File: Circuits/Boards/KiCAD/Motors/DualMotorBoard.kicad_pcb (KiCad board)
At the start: 2 copper layers, 127 x 101.6 mm, 96 parts, among them J1 Conn_01x05, J10 Conn_01x01, J11 Conn_01x01, J12 Conn_01x01, J13 Conn_01x01, J14 Conn_01x01, J2 Conn_01x01, J3 Conn_01x01, J4 Conn_01x01, J5 Conn_01x01, J6 Conn_01x01, J7 Conn_01x01, J8 Conn_01x05, J9 Conn_01x01, Q1 2N3904, Q10 Q_NMOS_DGS, Q11 Q_NMOS_DGS, Q12 Q_NMOS_DGS, Q13 Q_NMOS_DGS, Q14 2N3904, Q15 2N3904, Q16 2N3904, Q17 2N3904, Q18 2N3904, Q19 2N3904, Q2 2N3904, Q20 2N3904, Q21 2N3904, Q22 2N3904, Q23 Q_NMOS_DGS, Q24 Q_NMOS_DGS, Q25 Q_NMOS_DGS, Q26 Q_NMOS_DGS, Q3 2N3904, Q4 2N3904, Q5 2N3904, Q6 2N3904, Q7 2N3904, Q8 2N3904, Q9 2N3904

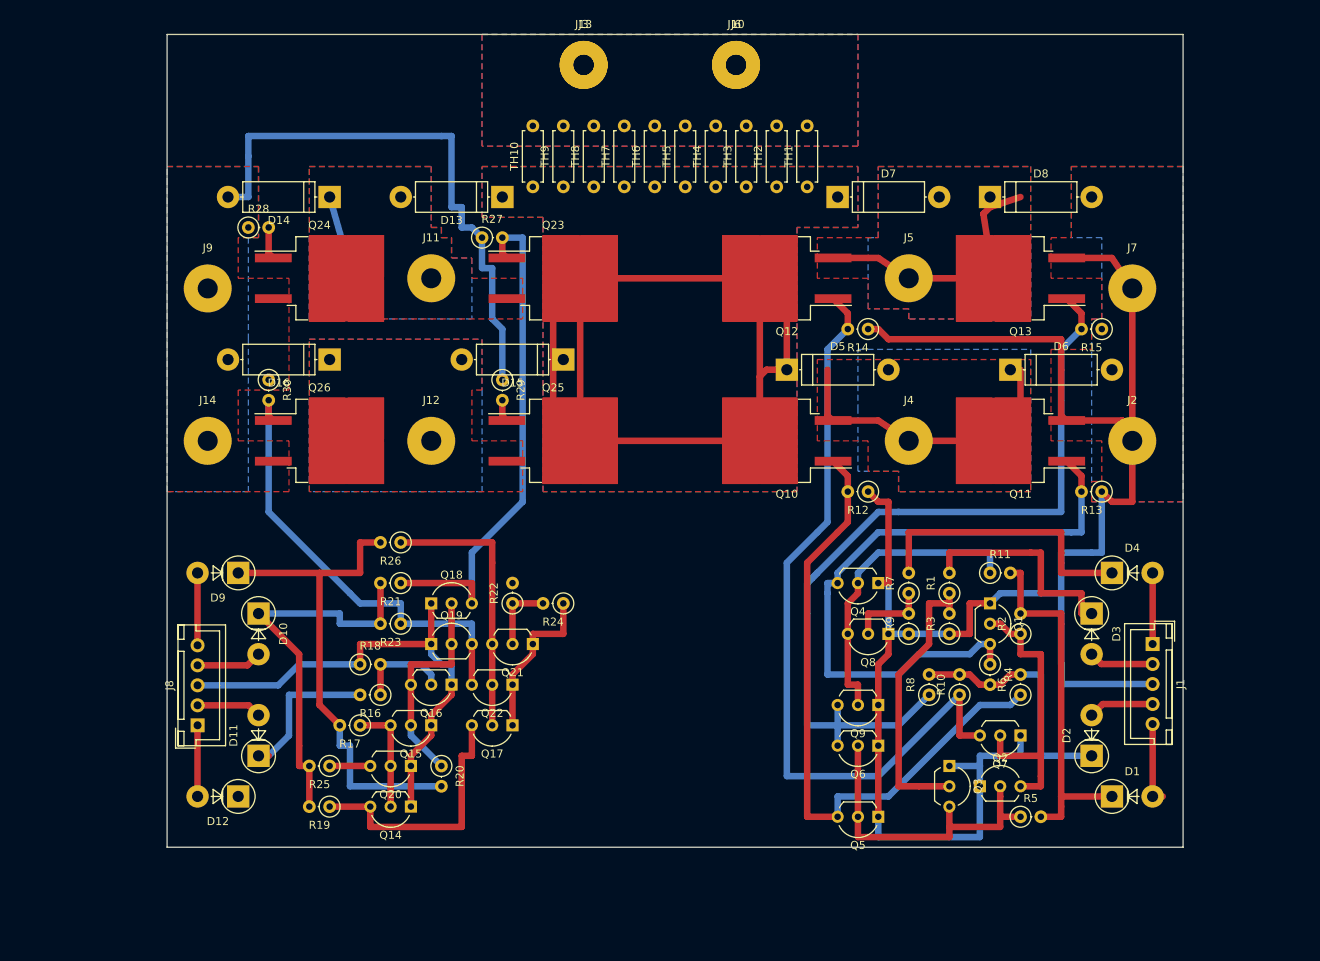
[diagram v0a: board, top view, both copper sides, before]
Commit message: Finished routing dual motor controller, needs to be cleaned up
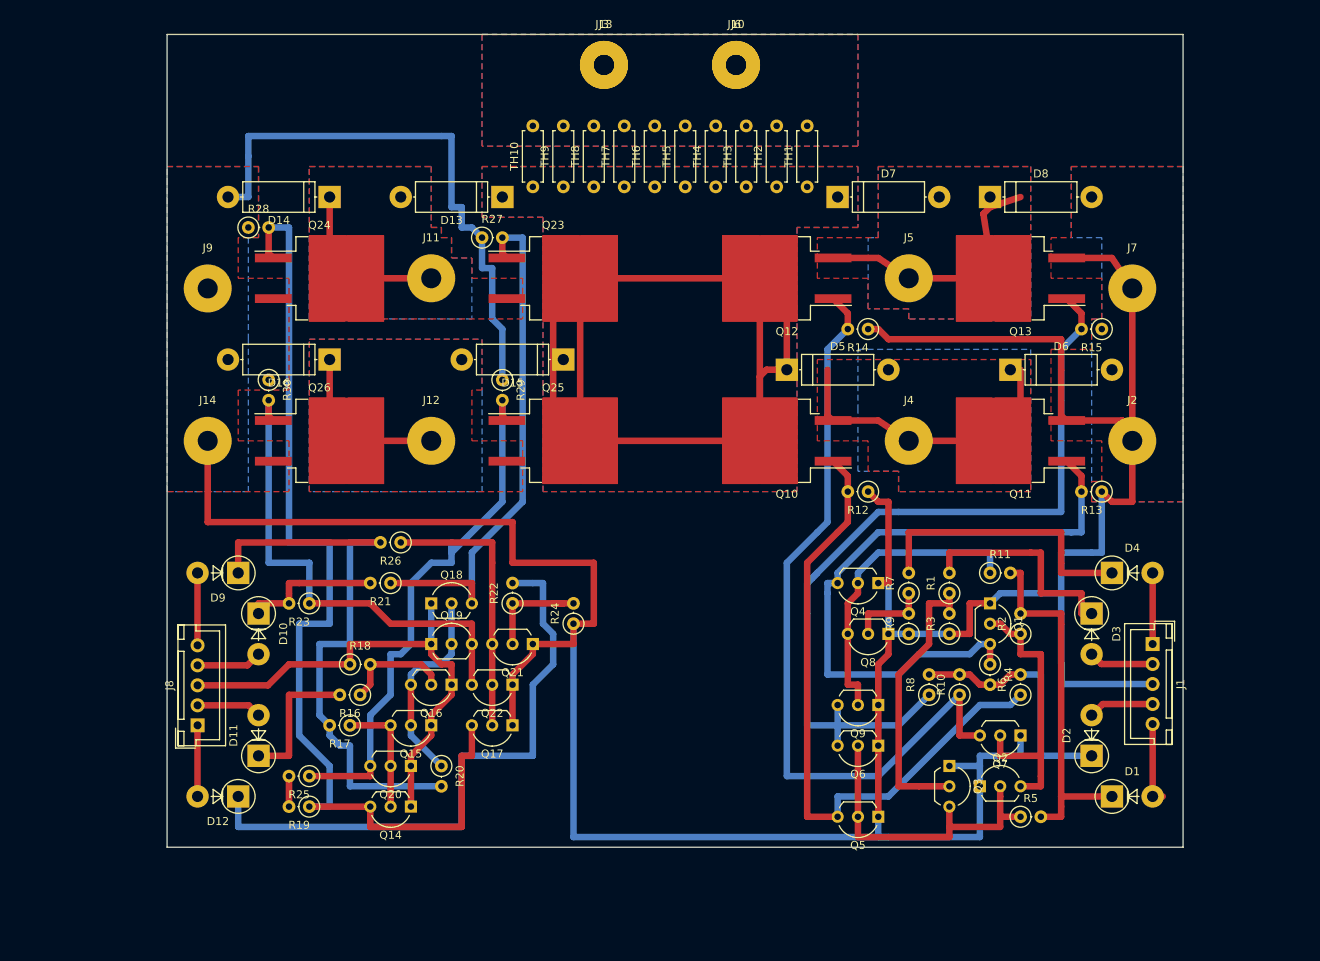
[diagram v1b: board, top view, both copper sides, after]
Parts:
- moved R23 11.7 mm to (144.8, 96.5)
- moved R24 2.84 mm to (177.8, 99.1), turned to 90 degrees
- moved R25 2.84 mm to (144.8, 118.1)
- moved J13 2.54 mm to (181.6, 29.2)
- moved J3 2.54 mm to (181.6, 29.2)
- moved R16 2.54 mm to (151.1, 108.0)
- moved R19 2.54 mm to (144.8, 121.9)
- moved R21 1.27 mm to (154.9, 94.0)
- moved R17 1.27 mm to (149.9, 111.8)
- moved R18 1.27 mm to (149.9, 104.1)
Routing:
- net GND: track 392.9 -> 531.3 mm
- net /MotorControlUnit_2/BBM: track 37.1 -> 127.5 mm
- net /MotorControlUnit_2/Speed: track 0.00 -> 76.5 mm
- net /MotorControlUnit_2/MBF: track 7.86 -> 69.0 mm
- net /MotorControlUnit_2/VG: track 49.1 -> 21.6 mm
- net /MotorControlUnit_2/VB: track 0.00 -> 21.6 mm
- net /MotorControlUnit_2/VF: track 9.25 -> 21.6 mm
- net /MotorControlUnit_2/VSW: track 62.0 -> 73.4 mm
- net /MotorControlUnit_2/FBM: track 57.0 -> 62.3 mm
- net /MotorControlUnit_2/SpeedSel: track 8.89 -> 14.0 mm
- net /MotorControlUnit_2/DirSel: track 12.0 -> 13.8 mm
- net /MotorControlUnit_2/MFB: track 27.0 -> 25.5 mm
- net /MotorControlUnit_2/MFF: track 65.1 -> 66.4 mm
- net /MotorControlUnit_2/MBB: track 14.0 -> 15.2 mm

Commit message: Added 26V and 5V units to the Dual motor controller board
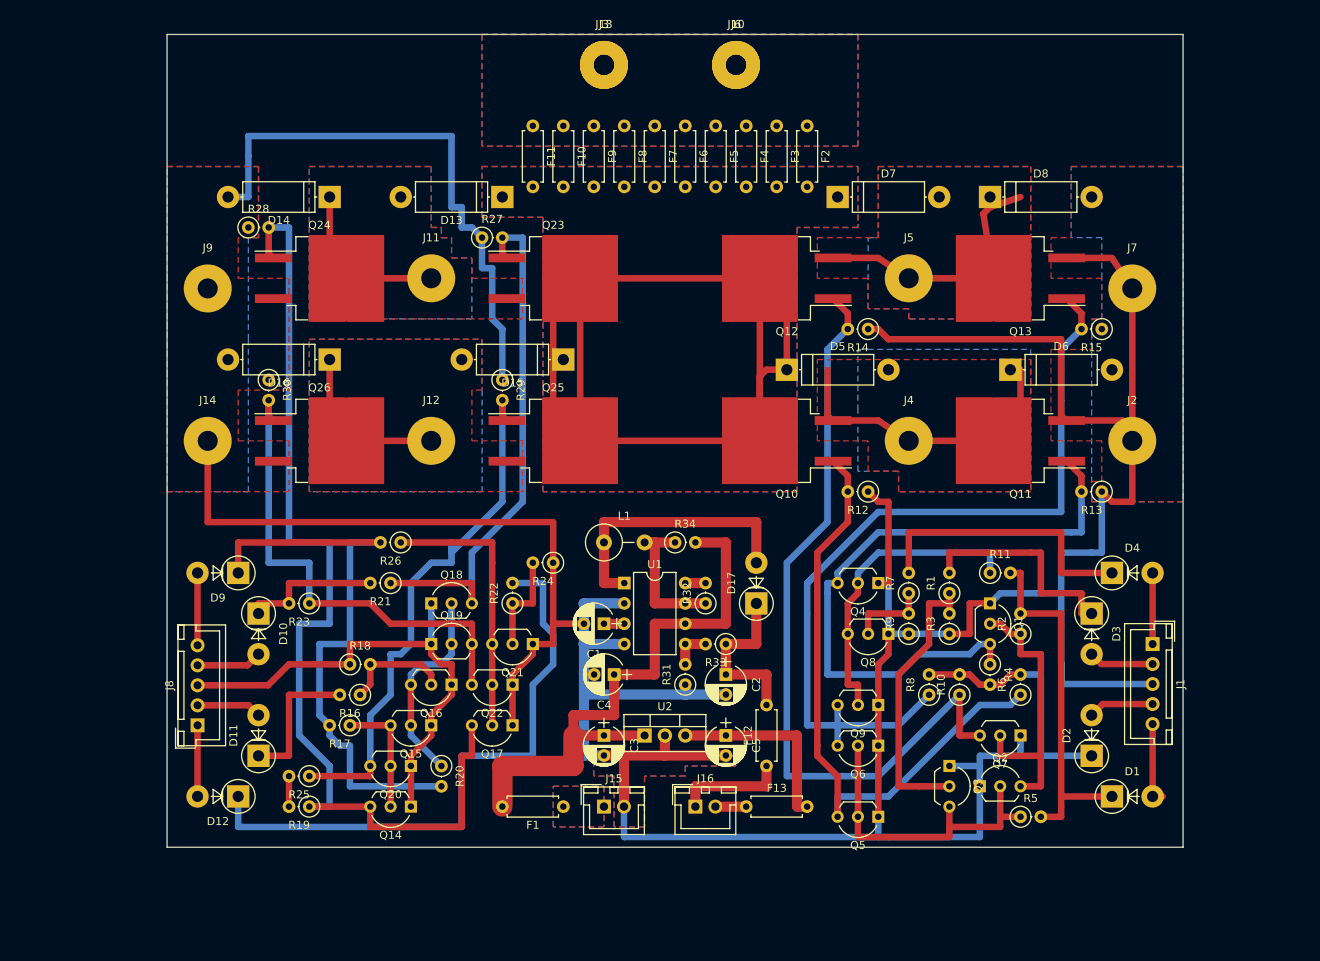
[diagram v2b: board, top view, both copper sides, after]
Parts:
- removed TH1, TH10, TH2, TH3, TH4, TH5, TH6, TH7, TH8, TH9: Thermistor_PTC, Resistors_THT:R_Axial_DIN0207_L6.3mm_D2.5mm_P7.62mm_Horizontal
- added C1: 470pF, Capacitors_THT:CP_Radial_D5.0mm_P2.50mm, F.Cu at (181.6, 99.1)
- added C2: 470uF, Capacitors_THT:CP_Radial_D5.0mm_P2.50mm, F.Cu at (196.8, 105.4)
- added C3: 100uF, Capacitors_THT:CP_Radial_D5.0mm_P2.50mm, F.Cu at (181.6, 113.0)
- added C4: 0.33uF, Capacitors_THT:CP_Radial_D5.0mm_P2.50mm, F.Cu at (182.9, 105.4)
- added C5: 0.1uF, Capacitors_THT:CP_Radial_D5.0mm_P2.50mm, F.Cu at (196.8, 113.0)
- added D17: 1N4007, Diodes_THT:D_5W_P5.08mm_Vertical_AnodeUp, F.Cu at (200.7, 96.5)
- added F1: Polyfuse, Resistors_THT:R_Axial_DIN0207_L6.3mm_D2.5mm_P7.62mm_Horizontal, F.Cu at (176.5, 121.9)
- added F10: Polyfuse, Resistors_THT:R_Axial_DIN0207_L6.3mm_D2.5mm_P7.62mm_Horizontal, F.Cu at (176.5, 36.8)
- added F11: Polyfuse, Resistors_THT:R_Axial_DIN0207_L6.3mm_D2.5mm_P7.62mm_Horizontal, F.Cu at (172.7, 36.8)
- added F12: Polyfuse, Resistors_THT:R_Axial_DIN0207_L6.3mm_D2.5mm_P7.62mm_Horizontal, F.Cu at (201.9, 116.8)
- added F13: Polyfuse, Resistors_THT:R_Axial_DIN0207_L6.3mm_D2.5mm_P7.62mm_Horizontal, F.Cu at (199.4, 121.9)
- added F2: Polyfuse, Resistors_THT:R_Axial_DIN0207_L6.3mm_D2.5mm_P7.62mm_Horizontal, F.Cu at (207.0, 36.8)
- added F3: Polyfuse, Resistors_THT:R_Axial_DIN0207_L6.3mm_D2.5mm_P7.62mm_Horizontal, F.Cu at (203.2, 36.8)
- added F4: Polyfuse, Resistors_THT:R_Axial_DIN0207_L6.3mm_D2.5mm_P7.62mm_Horizontal, F.Cu at (199.4, 36.8)
- added F5: Polyfuse, Resistors_THT:R_Axial_DIN0207_L6.3mm_D2.5mm_P7.62mm_Horizontal, F.Cu at (195.6, 36.8)
- added F6: Polyfuse, Resistors_THT:R_Axial_DIN0207_L6.3mm_D2.5mm_P7.62mm_Horizontal, F.Cu at (191.8, 36.8)
- added F7: Polyfuse, Resistors_THT:R_Axial_DIN0207_L6.3mm_D2.5mm_P7.62mm_Horizontal, F.Cu at (188.0, 36.8)
- added F8: Polyfuse, Resistors_THT:R_Axial_DIN0207_L6.3mm_D2.5mm_P7.62mm_Horizontal, F.Cu at (184.2, 36.8)
- added F9: Polyfuse, Resistors_THT:R_Axial_DIN0207_L6.3mm_D2.5mm_P7.62mm_Horizontal, F.Cu at (180.3, 36.8)
- added J15: Conn_01x02, Connectors_JST:JST_XH_B02B-XH-A_02x2.50mm_Straight, F.Cu at (181.6, 121.9)
- added J16: Conn_01x02, Connectors_JST:JST_XH_B02B-XH-A_02x2.50mm_Straight, F.Cu at (193.0, 121.9)
- added L1: 150uH, Inductors_THT:L_Axial_L11.0mm_D4.5mm_P5.08mm_Vertical_Fastron_MECC, F.Cu at (181.6, 88.9)
- added R31: 1K, Resistors_THT:R_Axial_DIN0207_L6.3mm_D2.5mm_P2.54mm_Vertical, F.Cu at (191.8, 106.7)
- added R32: 1K, Resistors_THT:R_Axial_DIN0207_L6.3mm_D2.5mm_P2.54mm_Vertical, F.Cu at (194.3, 96.5)
- added R33: 20K, Resistors_THT:R_Axial_DIN0207_L6.3mm_D2.5mm_P2.54mm_Vertical, F.Cu at (196.8, 101.6)
- added R34: 0.22, Resistors_THT:R_Axial_DIN0207_L6.3mm_D2.5mm_P2.54mm_Vertical, F.Cu at (190.5, 88.9)
- added U1: MC34063, Housings_DIP:DIP-8_W7.62mm, F.Cu at (184.2, 94.0)
- added U2: LM7805_TO220, TO_SOT_Packages_THT:TO-220-3_Vertical, F.Cu at (186.7, 113.0)
- moved R24 8.03 mm to (175.3, 91.4), turned to 180 degrees
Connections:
- net VFuse renamed /MotorControlUnit_1/VFUSE
- D1 pad 1: /MotorControlUnit_1/VSW -> /MotorControlUnit_1/DVSW
- D1 pad 2: Net-(D1-Pad2) -> /MotorControlUnit_1/VSW
- D10 pad 1: /MotorControlUnit_2/VG -> /MotorControlUnit_2/DVG
- D10 pad 2: Net-(D10-Pad2) -> /MotorControlUnit_2/VG
- D2 pad 1: /MotorControlUnit_1/VG -> /MotorControlUnit_1/DVG
- D2 pad 2: Net-(D2-Pad2) -> /MotorControlUnit_1/VG
- D9 pad 1: /MotorControlUnit_2/VSW -> /MotorControlUnit_2/DVSW
- D9 pad 2: Net-(D9-Pad2) -> /MotorControlUnit_2/VSW
- J1 pad 4: Net-(D2-Pad2) -> /MotorControlUnit_1/VG
- J1 pad 5: Net-(D1-Pad2) -> /MotorControlUnit_1/VSW
- J8 pad 4: Net-(D10-Pad2) -> /MotorControlUnit_2/VG
- J8 pad 5: Net-(D9-Pad2) -> /MotorControlUnit_2/VSW
- R10 pad 2: /MotorControlUnit_1/VG -> /MotorControlUnit_1/DVG
- R11 pad 2: /MotorControlUnit_1/VSW -> /MotorControlUnit_1/DVSW
- R17 pad 2: /MotorControlUnit_2/VSW -> /MotorControlUnit_2/DVSW
- R19 pad 2: /MotorControlUnit_2/VG -> /MotorControlUnit_2/DVG
- R2 pad 2: /MotorControlUnit_1/VSW -> /MotorControlUnit_1/DVSW
- R20 pad 2: /MotorControlUnit_2/VSW -> /MotorControlUnit_2/DVSW
- R21 pad 2: /MotorControlUnit_2/VG -> /MotorControlUnit_2/DVG
- R23 pad 2: /MotorControlUnit_2/VG -> /MotorControlUnit_2/DVG
- R25 pad 2: /MotorControlUnit_2/VG -> /MotorControlUnit_2/DVG
- R26 pad 2: /MotorControlUnit_2/VSW -> /MotorControlUnit_2/DVSW
- R4 pad 2: /MotorControlUnit_1/VG -> /MotorControlUnit_1/DVG
- R5 pad 2: /MotorControlUnit_1/VSW -> /MotorControlUnit_1/DVSW
- R6 pad 2: /MotorControlUnit_1/VG -> /MotorControlUnit_1/DVG
- R8 pad 2: /MotorControlUnit_1/VG -> /MotorControlUnit_1/DVG
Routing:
- net /26VUnit/VIN: track 0.00 -> 73.7 mm
- net /MotorControlUnit_2/DVSW: track 0.00 -> 73.4 mm
- net /MotorControlUnit_2/VSW: track 73.4 -> 9.05 mm
- net /MotorControlUnit_1/DVSW: track 0.00 -> 45.7 mm
- net GND: track 531.3 -> 570.9 mm
- net /MotorControlUnit_1/VSW: track 45.7 -> 10.3 mm
- net /26VUnit/N$5: track 0.00 -> 34.3 mm
- net /MotorControlUnit_1/DVG: track 0.00 -> 31.5 mm
- net /5VUnit/VOUT: track 0.00 -> 24.1 mm
- net /MotorControlUnit_1/VG: track 31.5 -> 8.20 mm
- net /26VUnit/VOUT: track 0.00 -> 21.6 mm
- net /MotorControlUnit_2/DVG: track 0.00 -> 21.6 mm
- net /26VUnit/N$12: track 0.00 -> 17.8 mm
- net Net-(F12-Pad1): track 0.00 -> 14.0 mm
- net /MotorControlUnit_2/VG: track 21.6 -> 8.20 mm
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- added copper zone on B.Cu, net Net-(F1-Pad1)
- added copper zone on F.Cu, net Net-(F1-Pad1)

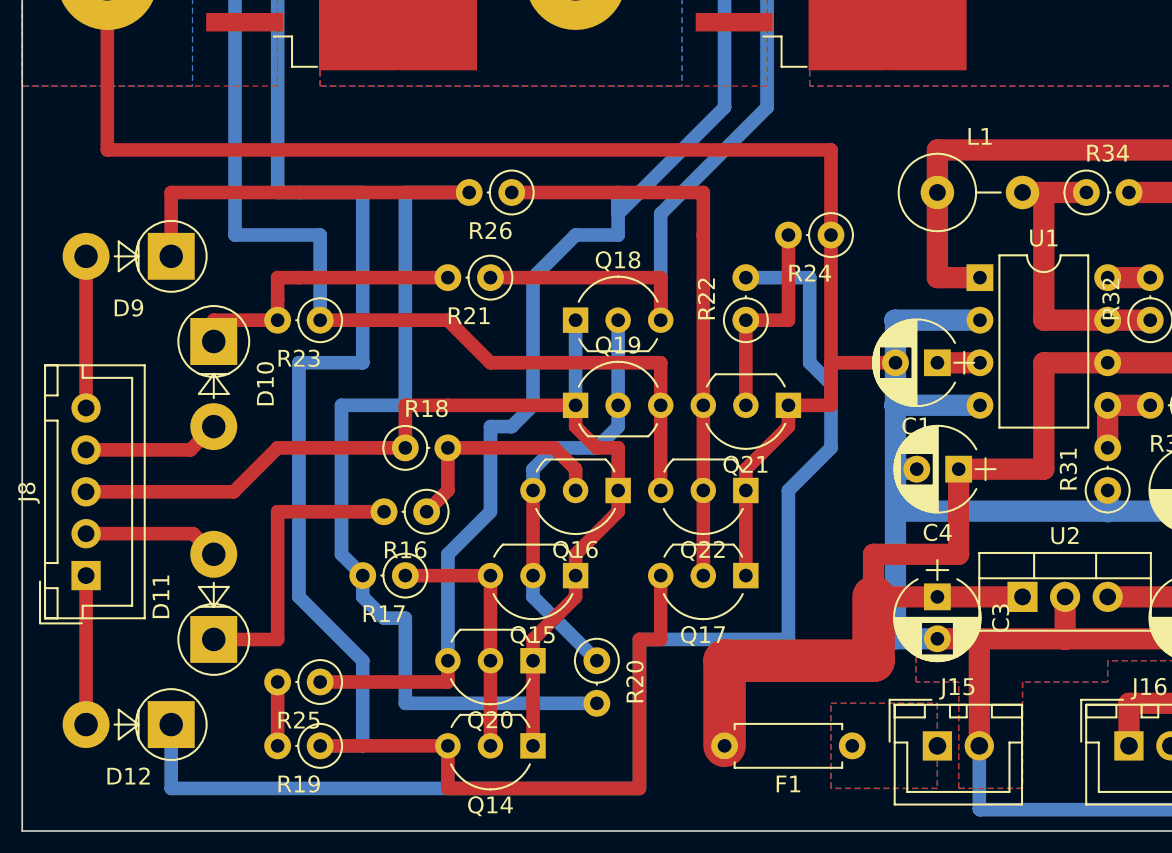
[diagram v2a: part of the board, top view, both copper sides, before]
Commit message: Fixed missing connections and routing
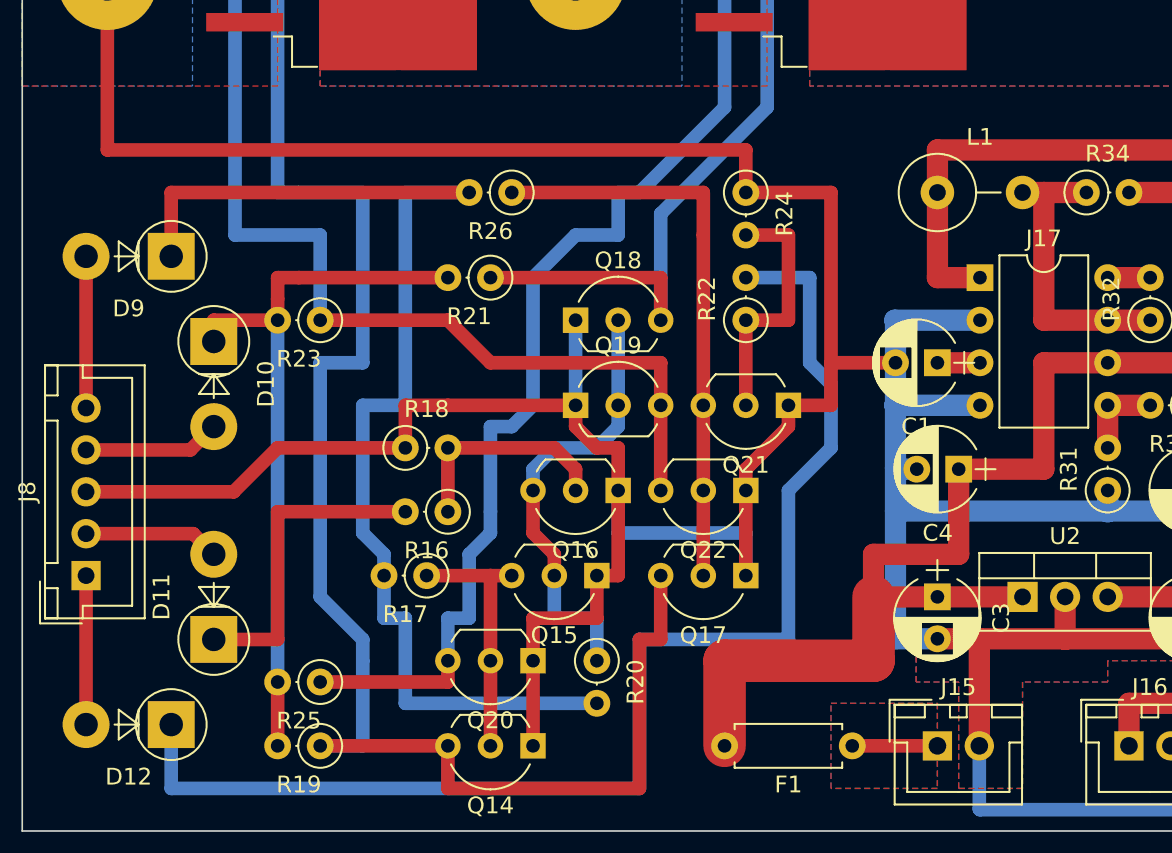
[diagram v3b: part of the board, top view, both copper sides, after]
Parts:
- removed U1: MC34063, Housings_DIP:DIP-8_W7.62mm
- added J17: MC34063, Housings_DIP:DIP-8_W7.62mm, F.Cu at (184.2, 94.0)
- moved R24 5.68 mm to (170.2, 88.9), turned to 270 degrees
- moved R16 1.27 mm to (152.4, 108.0)
- moved Q15 1.27 mm to (161.3, 111.8)
- moved R17 1.27 mm to (151.1, 111.8)
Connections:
- net +15V renamed +BATT
- R32 pad 2: /26VUnit/N$11 -> Net-(J17-Pad8)
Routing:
- net /MotorControlUnit_2/DVG: track 21.6 -> 43.2 mm
- net GND: track 570.9 -> 586.6 mm
- net Net-(F1-Pad1): track 0.00 -> 5.08 mm
- net Net-(J17-Pad8): track 0.00 -> 2.54 mm
- net /MotorControlUnit_2/SpeedSel: track 12.7 -> 15.2 mm
- net /26VUnit/N$11: track 2.54 -> 0.00 mm
- net /MotorControlUnit_2/BBM: track 127.5 -> 125.8 mm
- net /MotorControlUnit_2/DVSW: track 73.4 -> 71.6 mm
- net /MotorControlUnit_2/MFB: track 25.5 -> 27.0 mm
- net /MotorControlUnit_2/Dir: track 19.0 -> 20.3 mm
- net /MotorControlUnit_2/MBF: track 69.0 -> 67.9 mm
- net /MotorControlUnit_2/DirSel: track 13.8 -> 13.2 mm
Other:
- rule via_min_size: 0.889 -> 0.8128
